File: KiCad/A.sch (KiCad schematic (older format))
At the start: 6 parts, among them U1 LM321

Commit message: update schematics and libraries
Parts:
- Ra1: renamed from Ra; value R -> Ra
- Rb1: renamed from Rb; value R -> Rb
- gave numbers to parts that had none: 1
- renumbered Rb to Rb2, Ra to a
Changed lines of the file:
@@
 $EndComp
 $Comp
-L Device:Speaker LS?
+L Device:Speaker LS1
 U 1 1 6177E562
 P 3300 1500
-F 0 "LS?" H 3470 1496 50  0000 L CNN
+F 0 "LS1" H 3470 1496 50  0000 L CNN
 F 1 "Speaker" H 3470 1405 50  0000 L CNN
 F 2 "" H 3300 1300 50  0001 C CNN
@@
 	2900 1600 2900 1900
 $Comp
-L power:GND #PWR?
+L power:GND #PWR04
 U 1 1 6177EBEA
 P 2900 1900
-F 0 "#PWR?" H 2900 1650 50  0001 C CNN
+F 0 "#PWR04" H 2900 1650 50  0001 C CNN
 F 1 "GND" H 2905 1727 50  0000 C CNN
 F 2 "" H 2900 1900 50  0001 C CNN
@@
 	2550 1500 2300 1500
 $Comp
-L Device:R Rb
+L Device:R Rb2
 U 1 1 6177F169
 P 2550 1800
-F 0 "Rb" H 2620 1846 50  0000 L CNN
-F 1 "Ra" H 2620 1755 50  0001 L CNN
+F 0 "Rb2" H 2620 1846 50  0001 L CNN
+F 1 "Ra" H 2600 1800 50  0000 L CNN
 F 2 "" V 2480 1800 50  0001 C CNN
 F 3 "~" H 2550 1800 50  0001 C CNN
@@
 	1550 1600 1700 1600
 $Comp
-L Device:R Ra
+L Device:R a
 U 1 1 6177F4BE
 P 2550 2350
-F 0 "Ra" H 2620 2396 50  0000 L CNN
-F 1 "Rb" H 2620 2305 50  0001 L CNN
+F 0 "a" H 2620 2396 50  0001 L CNN
+F 1 "Rb" H 2600 2350 50  0000 L CNN
 F 2 "" V 2480 2350 50  0001 C CNN
 F 3 "~" H 2550 2350 50  0001 C CNN
@@
 	2550 2500 2550 2550
 $Comp
-L power:GND #PWR?
+L power:GND #PWR03
 U 1 1 6177FBF4
 P 2550 2550
-F 0 "#PWR?" H 2550 2300 50  0001 C CNN
+F 0 "#PWR03" H 2550 2300 50  0001 C CNN
 F 1 "GND" H 2555 2377 50  0000 C CNN
 F 2 "" H 2550 2550 50  0001 C CNN
@@
 in
 $Comp
-L Device:R Ra
+L Device:R Ra1
 U 1 1 6178AA2F
 P 1200 1400
-F 0 "Ra" V 1085 1400 50  0000 C CNN
-F 1 "R" V 1084 1400 50  0001 C CNN
+F 0 "Ra1" V 1085 1400 50  0001 C CNN
+F 1 "Ra" V 1100 1400 50  0000 C CNN
 F 2 "" V 1130 1400 50  0001 C CNN
 F 3 "~" H 1200 1400 50  0001 C CNN
@@
 Wire Wire Line
 	1500 1400 1350 1400
-$Comp
-L Device:R Rb
-U 1 1 6178C9AA
-P 1500 1050
-F 0 "Rb" H 1570 1050 50  0000 L CNN
-F 1 "R" H 1570 1005 50  0001 L CNN
-F 2 "" V 1430 1050 50  0001 C CNN
-F 3 "~" H 1500 1050 50  0001 C CNN
-	1    1500 1050
-	1    0    0    -1
-$EndComp
 Wire Wire Line
 	1500 900  1500 750
@@
 	1900 1200 1900 1150
 $Comp
-L power:VCC #PWR?
+L power:VCC #PWR01
 U 1 1 6178D2C8
 P 1900 1150
-F 0 "#PWR?" H 1900 1000 50  0001 C CNN
+F 0 "#PWR01" H 1900 1000 50  0001 C CNN
 F 1 "VCC" H 1917 1323 50  0000 C CNN
 F 2 "" H 1900 1150 50  0001 C CNN
@@
 	1900 1800 1900 1850
 $Comp
-L power:GND #PWR?
+L power:GND #PWR02
 U 1 1 6178D6E5
 P 1900 1850
-F 0 "#PWR?" H 1900 1600 50  0001 C CNN
+F 0 "#PWR02" H 1900 1600 50  0001 C CNN
 F 1 "GND" H 1905 1677 50  0000 C CNN
 F 2 "" H 1900 1850 50  0001 C CNN
@@
 Wire Wire Line
 	2550 1500 3100 1500
+$Comp
+L Device:R Rb1
+U 1 1 6178C9AA
+P 1500 1050
+F 0 "Rb1" H 1570 1050 50  0001 L CNN
+F 1 "Rb" H 1550 1050 50  0000 L CNN
+F 2 "" V 1430 1050 50  0001 C CNN
+F 3 "Rb" H 1500 1050 50  0001 C CNN
+	1    1500 1050
+	1    0    0    -1
+$EndComp
 $EndSCHEMATC

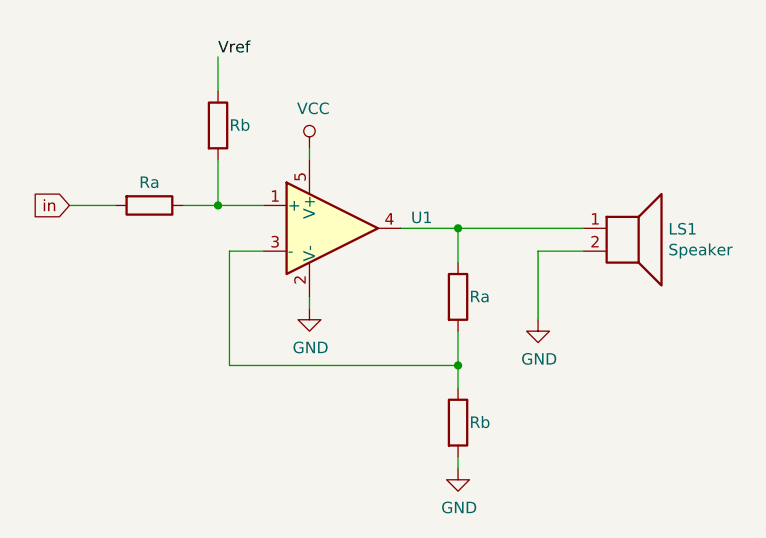
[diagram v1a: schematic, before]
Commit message: corrected opamp circuits
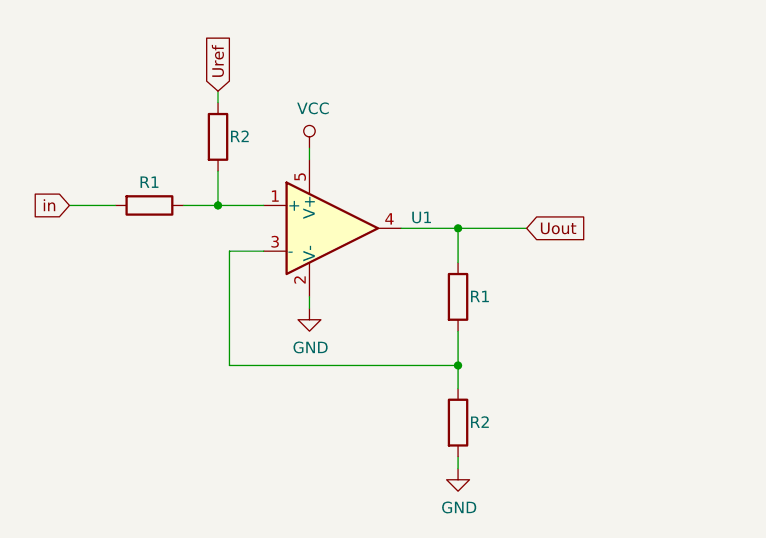
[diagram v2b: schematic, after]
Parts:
- removed LS1: Speaker, symbol Device:Speaker
- Ra1, Rb2: value Ra -> R1
- Rb1: value Rb -> R2
- a1: renamed from a; value Rb -> R2
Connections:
- net Uout: now reaches Rb2.1, U1.4
- net Vref renamed Uref
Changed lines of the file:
@@
-	1    0    0    -1
-$EndComp
-$Comp
-L Device:Speaker LS1
-U 1 1 6177E562
-P 3300 1500
-F 0 "LS1" H 3470 1496 50  0000 L CNN
-F 1 "Speaker" H 3470 1405 50  0000 L CNN
-F 2 "" H 3300 1300 50  0001 C CNN
-F 3 "~" H 3290 1450 50  0001 C CNN
-	1    3300 1500
-	1    0    0    -1
-$EndComp
-Wire Wire Line
-	3100 1600 2900 1600
-Wire Wire Line
-	2900 1600 2900 1900
-$Comp
-L power:GND #PWR04
-U 1 1 6177EBEA
-P 2900 1900
-F 0 "#PWR04" H 2900 1650 50  0001 C CNN
-F 1 "GND" H 2905 1727 50  0000 C CNN
-F 2 "" H 2900 1900 50  0001 C CNN
-F 3 "" H 2900 1900 50  0001 C CNN
-	1    2900 1900
 	1    0    0    -1
 $EndComp
 Wire Wire Line
 	2550 1500 2550 1650
-Connection ~ 2550 1500
 Wire Wire Line
 	2550 1500 2300 1500
@@
 P 2550 1800
 F 0 "Rb2" H 2620 1846 50  0001 L CNN
-F 1 "Ra" H 2600 1800 50  0000 L CNN
+F 1 "R1" H 2600 1800 50  0000 L CNN
 F 2 "" V 2480 1800 50  0001 C CNN
 F 3 "~" H 2550 1800 50  0001 C CNN
@@
 	1550 1600 1700 1600
 $Comp
-L Device:R a
+L Device:R a1
 U 1 1 6177F4BE
 P 2550 2350
-F 0 "a" H 2620 2396 50  0001 L CNN
-F 1 "Rb" H 2600 2350 50  0000 L CNN
+F 0 "a1" H 2620 2396 50  0001 L CNN
+F 1 "R2" H 2600 2350 50  0000 L CNN
 F 2 "" V 2480 2350 50  0001 C CNN
 F 3 "~" H 2550 2350 50  0001 C CNN
@@
 P 1200 1400
 F 0 "Ra1" V 1085 1400 50  0001 C CNN
-F 1 "Ra" V 1100 1400 50  0000 C CNN
+F 1 "R1" V 1100 1400 50  0000 C CNN
 F 2 "" V 1130 1400 50  0001 C CNN
 F 3 "~" H 1200 1400 50  0001 C CNN
@@
 	850  1400 1050 1400
 Wire Wire Line
-	1500 1400 1500 1200
+	1500 1400 1500 1250
 Connection ~ 1500 1400
 Wire Wire Line
 	1500 1400 1350 1400
 Wire Wire Line
-	1500 900  1500 750
-Text Label 1500 750  0    50   ~ 0
-Vref
+	1500 950  1500 900
 Wire Wire Line
 	1900 1200 1900 1150
@@
 	1    0    0    -1
 $EndComp
-Wire Wire Line
-	2550 1500 3100 1500
 $Comp
 L Device:R Rb1
 U 1 1 6178C9AA
-P 1500 1050
-F 0 "Rb1" H 1570 1050 50  0001 L CNN
-F 1 "Rb" H 1550 1050 50  0000 L CNN
-F 2 "" V 1430 1050 50  0001 C CNN
-F 3 "Rb" H 1500 1050 50  0001 C CNN
-	1    1500 1050
+P 1500 1100
+F 0 "Rb1" H 1570 1100 50  0001 L CNN
+F 1 "R2" H 1550 1100 50  0000 L CNN
+F 2 "" V 1430 1100 50  0001 C CNN
+F 3 "Rb" H 1500 1100 50  0001 C CNN
+	1    1500 1100
 	1    0    0    -1
 $EndComp
+Text GLabel 1500 900  1    50   Input ~ 0
+Uref
+Wire Wire Line
+	2550 1500 2850 1500
+Connection ~ 2550 1500
+Text GLabel 2850 1500 2    50   Input ~ 0
+Uout
 $EndSCHEMATC
